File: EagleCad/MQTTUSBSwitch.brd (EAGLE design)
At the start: 40 x 80 mm, 41 parts, among them J1 10117835-002LF, J2 GSB4211311WEU, Q1 MMBT2222, Q2 MMBT2222, Q3 MMBT2222, Q4 MMBT2222, U1 MIC5504-3.3YM5_TR, X2 MICROBUILDER_RELAY_LATCHINGEE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, X3 MICROBUILDER_RELAY_LATCHINGEE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

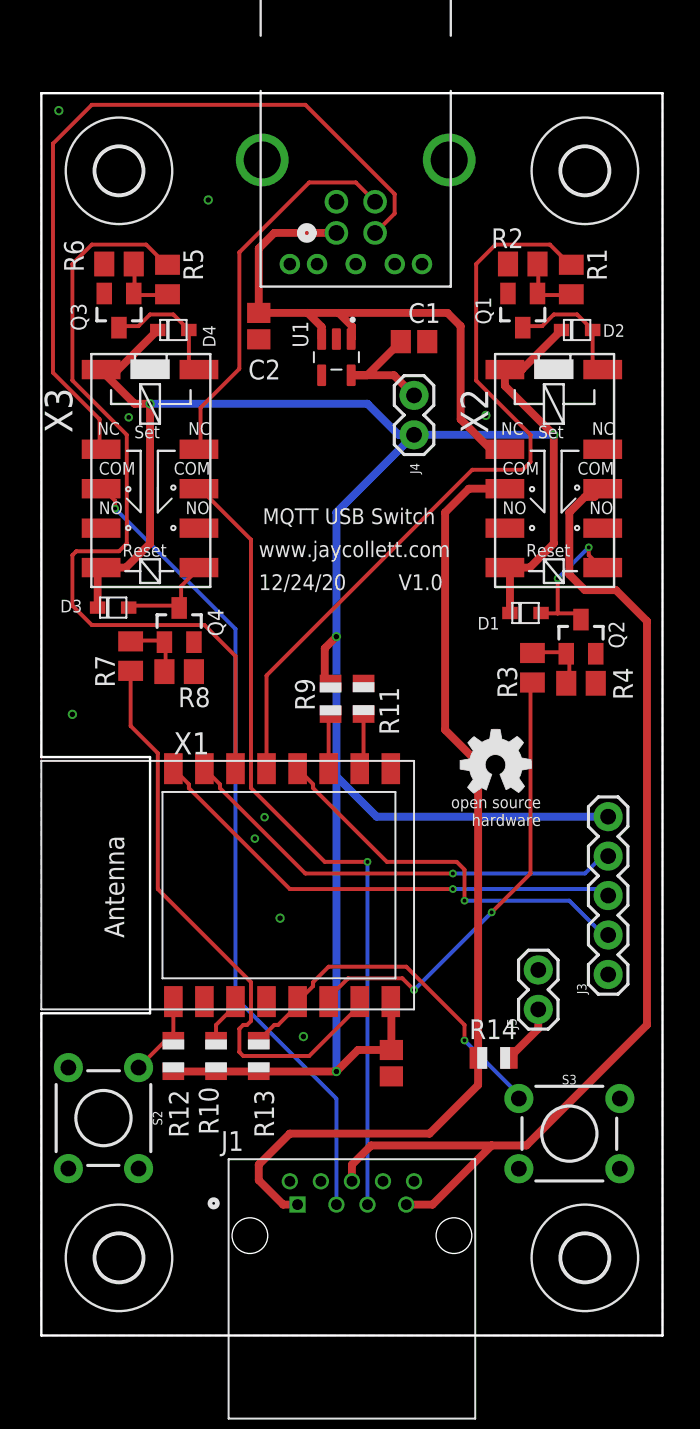
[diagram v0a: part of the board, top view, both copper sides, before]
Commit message: fix board issue with ground airwires and soldermask exposing ground plane
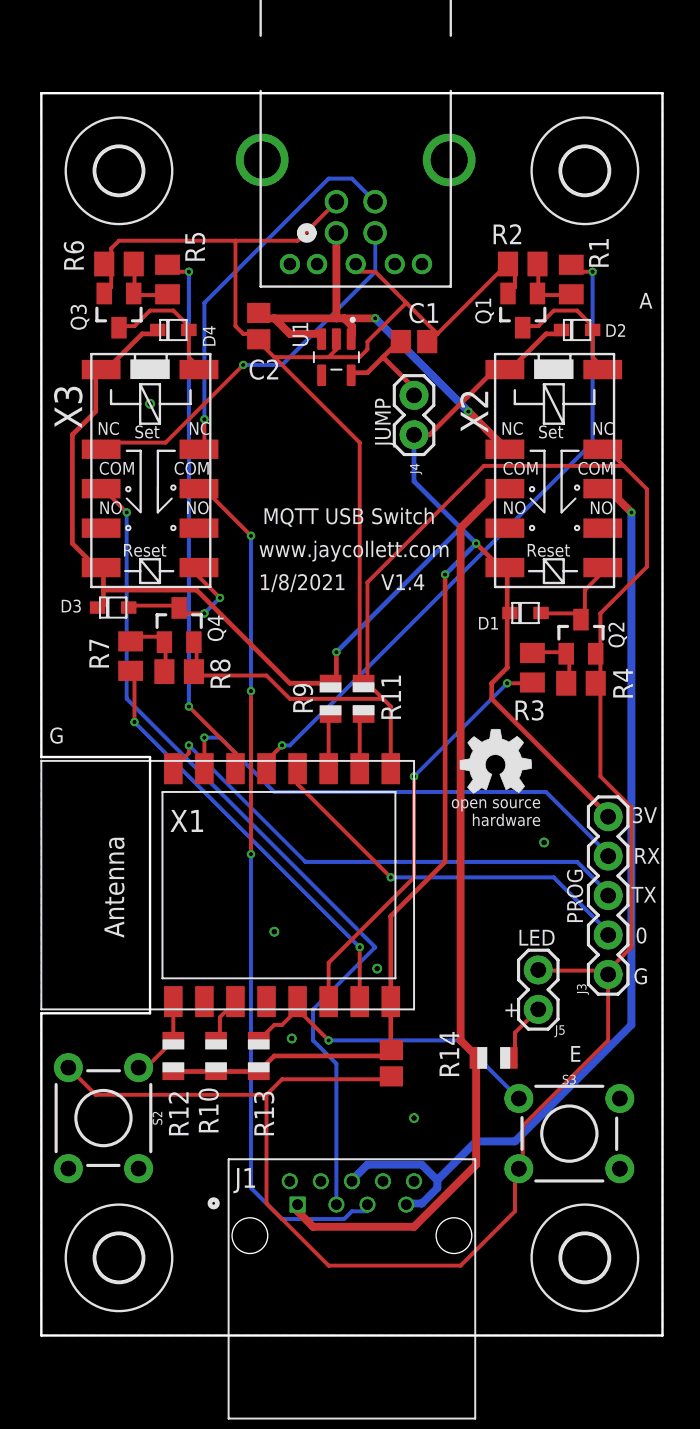
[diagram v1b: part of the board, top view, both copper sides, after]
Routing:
- net GND: track 0.00 -> 237.0 mm, vias 9 -> 6
- net D-: track 49.4 -> 25.0 mm, vias 0 -> 1
- net CONNECT_2: track 52.8 -> 34.8 mm, vias 0 -> 2
- net 3.3V: track 159.6 -> 146.7 mm, vias 4 -> 3
- net DISCONNECT_2: track 37.7 -> 27.4 mm, vias 0 -> 2
- net GND_USB_OUT: track 69.9 -> 61.5 mm, vias 0 -> 1
- net CONNECT: track 50.1 -> 42.6 mm, vias 0 -> 2
- net USB_5V_IN: track 36.7 -> 30.5 mm, vias 0 -> 2
- net D+_OUT: track 52.2 -> 55.6 mm, vias 1 -> 3
- net D-_OUT: track 52.4 -> 55.7 mm
- net USB_5V_OUT: track 62.6 -> 59.4 mm
- net N$11: track 9.63 -> 6.66 mm, vias 2 -> 0
- net MAN_SWITCH: track 23.3 -> 20.5 mm
- net N$15: track 6.48 -> 9.18 mm, vias 0 -> 2
- net DISCONNECT: track 29.6 -> 26.9 mm
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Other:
- board text added: "+"
- board text added: "0"
- board text added: "1/8/2021"
- board text added: "3V"
- board text added: "A"
- board text added: "E"
- board text added: "G"
- board text added: "JUMP"
- board text added: "LED"
- board text added: "PROG"
- board text added: "RX"
- board text added: "TX"
- board text added: "V1.4"
- board text removed: "12/24/20"
- board text removed: "V1.0"

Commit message: first pass at v2.1 which simplifies relay driving with a unla2803 and a port expander to only use 2 GPIO pins on ESP8266
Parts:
- removed D1, D2, D3, D4: 1N4148, adafruit:SOD-323F
- removed Q1, Q2, Q3, Q4: MMBT2222, MMBT2222_:SOT23-BEC
- removed R3, R5, R7: 1K, adafruit:M0805
- removed R4, R6, R8: 10K, adafruit:M0805
- removed X2, X3: MICROBUILDER_RELAY_LATCHINGEE2NUH, AdaFruitLatchingRelay:MICROBUILDER_RELAY_EE2_LATCH
- added IC1: ULN2803A, uln-udn:DIL18
- added IC2: MCP23008/P, adafruit:DIL18
- added K1, K2, K3, K4: EC2-3TNU, SamacSys_Parts:EC23TNU
- R1: value 1K -> 4.7k; device adafruit:M0805 -> adafruit:R0805
- R2: value 10K -> 4.7k; device adafruit:M0805 -> adafruit:R0805
- moved GOLD_ORB_SM1 57.9 mm to (-25.8, 18.8)
- moved R2 33.8 mm to (12.0, 41.0), turned to 90 degrees
- moved R1 33.1 mm to (15.0, 41.0), turned to 90 degrees
- moved H2 31.0 mm to (5.00, 106.0)
- moved H3 31.0 mm to (35.0, 106.0)
- moved J2 30.0 mm to (19.0, 101.0)
- moved J4 28.3 mm to (21.1, 86.1), turned to 0 degrees
- moved C1 28.0 mm to (24.0, 92.0)
- moved C2 28.0 mm to (14.0, 93.0)
- moved U1 28.0 mm to (19.0, 91.0)
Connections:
- removed net CONNECT: R1.1, X1.13
- removed net CONNECT_2: R5.1, X1.14
- removed net DISCONNECT: R3.1, X1.6
- removed net DISCONNECT_2: R7.1, X1.7
- removed net N$10: D2.A, Q1.C, X2.12
- removed net N$11: D1.A, Q2.C, X2.7
- removed net N$12: Q1.B, R1.2, R2.2
- removed net N$13: Q2.B, R3.2, R4.2
- removed net N$14: D4.A, Q3.C, X3.12
- removed net N$15: D3.A, Q4.C, X3.7
- removed net N$16: Q3.B, R5.2, R6.2
- removed net N$17: Q4.B, R7.2, R8.2
- new net N$2: IC1.1, IC2.10
- new net N$3: IC1.2, IC2.11
- new net N$4: IC1.3, IC2.12
- new net N$5: IC1.4, IC2.13
- new net N$6: IC1.5, IC2.14
- new net N$7: IC1.6, IC2.15
- new net N$8: IC1.7, IC2.16
- new net N$9: IC1.8, IC2.17
- new net SCL: IC2.1, R2.1, X1.14
- new net SDA: IC2.2, R1.1, X1.13
- new net SSRX+: J2.9, K3.3
- new net SSRX+_USB_OUT: J1.6, K3.4
- new net SSRX-: J2.8, K3.10
- new net SSRX-_USB_OUT: J1.5, K3.9
- new net SSTX+: J2.6, K4.3
- new net SSTX+_USB_OUT: J1.9, K4.4
- new net SSTX-: J2.5, K4.10
- new net SSTX-_USB_OUT: J1.8, K4.9
- new net USBDATA_CONNECT_COIL: IC1.16, K2.12
- new net USBDATA_DISCONNECT_COIL: IC1.15, K2.7
- new net USBPWR_CONNECT_COIL: IC1.18, K1.12
- new net USBPWR_DISCONNECT_COIL: IC1.17, K1.7
- new net USBSSRX_CONNECT_COIL: IC1.14, K3.12
- new net USBSSRX_DISCONNECT_COIL: IC1.13, K3.7
- new net USBSSTX_CONNECT_COIL: IC1.12, K4.12
- new net USBSSTX_DISCONNECT_COIL: IC1.11, K4.7
- net 3.3V: now also IC1.10, IC2.18, IC2.6, K1.1, K1.6, K2.1, K2.6, K3.1, K3.6, K4.1, K4.6, R1.2, R2.2; no longer D1.C, D2.C, D3.C, D4.C, X2.1, X2.6, X3.1, X3.6
- net D+: now also K2.4; no longer X3.10
- net D+_OUT: now also K2.3; no longer X3.9
- net D-: now also K2.9; no longer X3.3
- net D-_OUT: now also K2.10; no longer X3.4
- net GND: now also IC1.9, IC2.3, IC2.4, IC2.5, IC2.9, K1.10; no longer Q1.E, Q2.E, Q3.E, Q4.E, R2.1, R4.1, R6.1, R8.1, X2.10
- net GND_USB_OUT: now also K1.9; no longer X2.9
- net USB_5V_IN: now also K1.3; no longer X2.3
- net USB_5V_OUT: now also K1.4; no longer X2.4
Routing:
- net GND: track 237.0 -> 0.00 mm, vias 6 -> 0
- net 3.3V: track 146.7 -> 0.00 mm, vias 3 -> 0
- net GND_USB_OUT: track 61.5 -> 0.00 mm, vias 1 -> 0
- net USB_5V_OUT: track 59.4 -> 0.00 mm
- net D-_OUT: track 55.7 -> 0.00 mm, vias 1 -> 0
- net D+_OUT: track 55.6 -> 0.00 mm, vias 3 -> 0
- net CONNECT: track 42.6 -> 0.00 mm, vias 2 -> 0
- net CONNECT_2: track 34.8 -> 0.00 mm, vias 2 -> 0
- net TX: track 33.0 -> 0.00 mm, vias 1 -> 0
- net RX: track 31.2 -> 0.00 mm, vias 1 -> 0
- net USB_5V_IN: track 30.5 -> 0.00 mm, vias 2 -> 0
- net DISCONNECT_2: track 27.4 -> 0.00 mm, vias 2 -> 0
- net DISCONNECT: track 26.9 -> 0.00 mm, vias 2 -> 0
- net GPIO_0: track 25.1 -> 0.00 mm, vias 1 -> 0
- net D-: track 25.0 -> 0.00 mm, vias 1 -> 0
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- removed copper zone on layer 1, net GND
- removed copper zone on layer 16, net GND
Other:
- board size 40 x 80 mm -> 40 x 111 mm
- board text added: "1/12/2021"
- board text added: "V2.1"
- board text removed: "1/8/2021"
- board text removed: "A"
- board text removed: "E"
- board text removed: "V1.4"

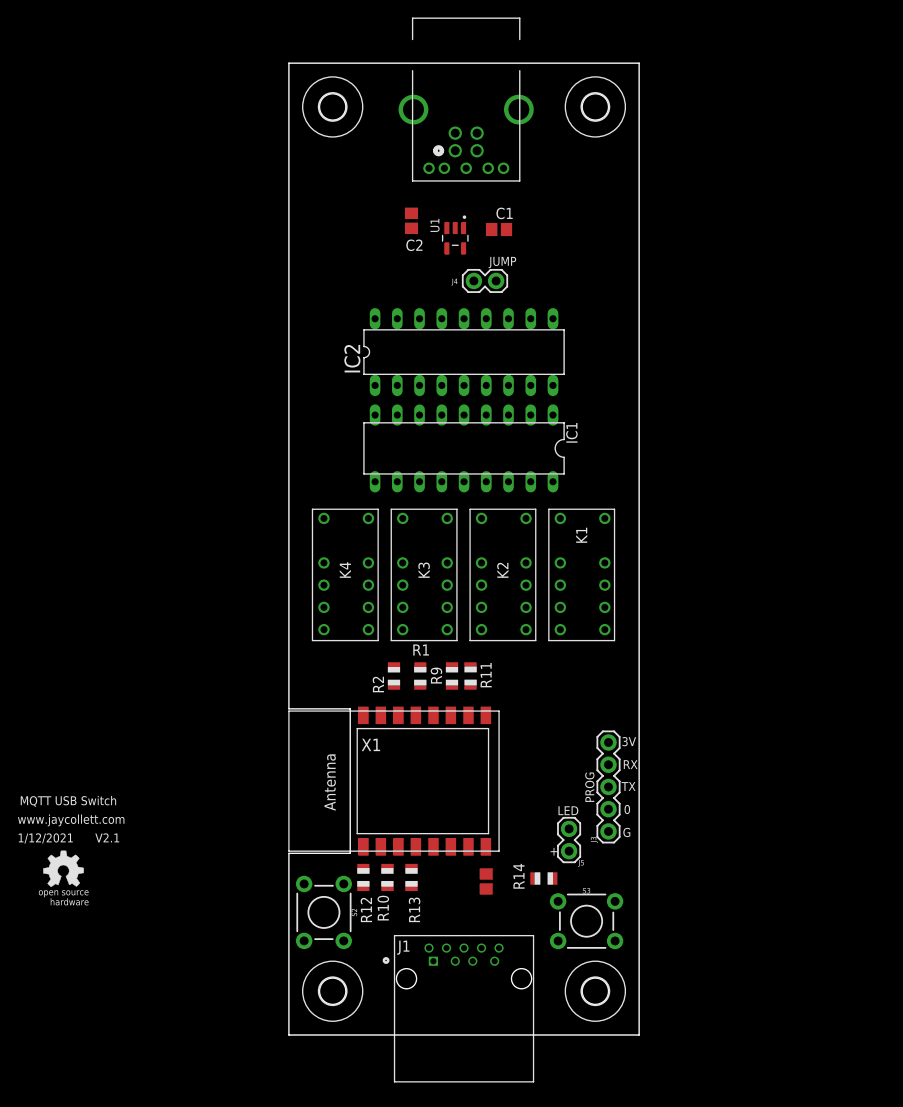
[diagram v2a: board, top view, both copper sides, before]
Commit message: New layout and routing for v2.1
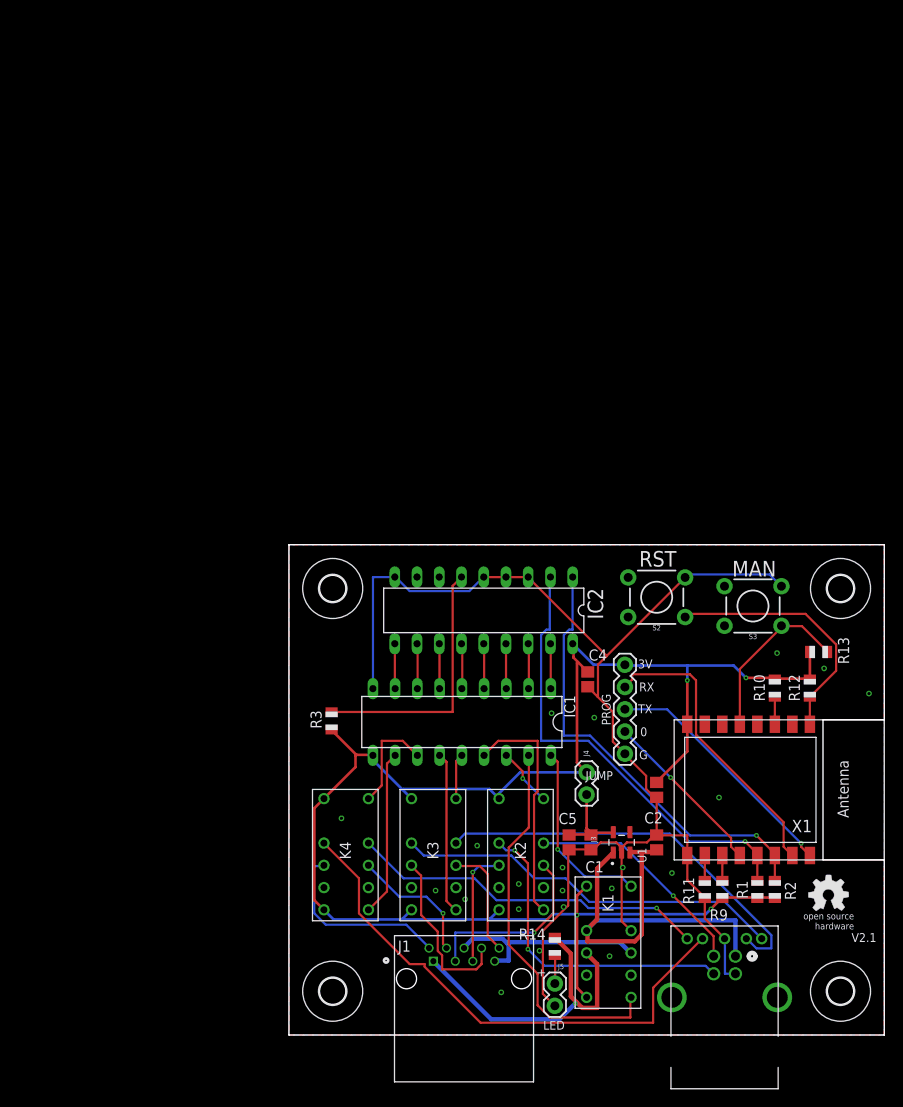
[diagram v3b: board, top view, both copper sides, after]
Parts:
- added C4, C5: (no value), adafruit:C0805
- added R3: 10k, adafruit:R0805
- moved J2 97.4 mm to (51.0, 9.00), turned to 0 degrees
- moved GOLD_ORB_SM1 87.4 mm to (61.6, 16.0)
- moved H2 79.9 mm to (63.0, 51.0)
- moved C2 76.3 mm to (42.0, 22.0), turned to 90 degrees
- moved U1 71.6 mm to (38.0, 22.0), turned to 90 degrees
- moved C1 70.8 mm to (34.5, 22.0), turned to 270 degrees
- moved H3 62.6 mm to (5.00, 51.0)
- moved J4 57.6 mm to (34.0, 30.0), turned to 270 degrees
- moved R12 55.4 mm to (59.5, 39.6), turned to 90 degrees
- moved R13 53.2 mm to (60.5, 43.8), turned to 180 degrees
- moved S2 52.3 mm to (42.0, 50.0), turned to 180 degrees
- moved R2 49.9 mm to (55.5, 16.6), turned to 270 degrees
- moved R10 49.3 mm to (55.5, 39.6), turned to 90 degrees
- moved R1 45.6 mm to (53.5, 16.6), turned to 270 degrees
- moved K1 42.1 mm to (34.0, 17.0)
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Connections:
- new net N$10: IC2.6, R3.1
- net 3.3V: now also C4.1, R3.2; no longer IC2.6
- net 3.3V_PRE_JUMP: now also C5.1
- net D+: now also K2.3; no longer K2.4
- net D+_OUT: now also K2.4; no longer K2.3
- net D-: now also K2.10; no longer K2.9
- net D-_OUT: now also K2.9; no longer K2.10
- net GND: now also C4.2, C5.2
- net N$2: now also IC1.8; no longer IC1.1
- net N$3: now also IC1.7; no longer IC1.2
- net N$4: now also IC1.6; no longer IC1.3
- net N$5: now also IC1.5; no longer IC1.4
- net N$6: now also IC1.4; no longer IC1.5
- net N$7: now also IC1.3; no longer IC1.6
- net N$8: now also IC1.2; no longer IC1.7
- net N$9: now also IC1.1; no longer IC1.8
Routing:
- net 3.3V: track 0.00 -> 189.9 mm, vias 0 -> 4
- net GND: track 0.00 -> 157.9 mm, vias 0 -> 21
- net SSTX+: track 0.00 -> 60.6 mm
- net SDA: track 0.00 -> 52.5 mm, vias 0 -> 1
- net USB_5V_IN: track 0.00 -> 52.3 mm
- net SCL: track 0.00 -> 51.5 mm, vias 0 -> 1
- net SSRX-: track 0.00 -> 46.1 mm
- net SSRX+: track 0.00 -> 44.5 mm
- net USBPWR_DISCONNECT_COIL: track 0.00 -> 44.4 mm
- net SSTX-: track 0.00 -> 40.9 mm, vias 0 -> 1
- net USB_5V_OUT: track 0.00 -> 37.7 mm, vias 0 -> 1
- net D+: track 0.00 -> 36.4 mm, vias 0 -> 2
- net RX: track 0.00 -> 33.9 mm
- net N$10: track 0.00 -> 29.7 mm
- net RST: track 0.00 -> 29.4 mm
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- added copper zone on layer 1, net GND
- added copper zone on layer 16, net GND
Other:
- board size 40 x 111 mm -> 68 x 56 mm
- board text added: "MAN"
- board text added: "RST"
